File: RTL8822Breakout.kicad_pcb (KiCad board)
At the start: 2 copper layers, 35 x 35 mm, 11 parts, among them J1 U.FL, J2 U.FL, J3 Conn_02x09_Odd_Even, J4 Conn_02x09_Odd_Even, U1 RTL8822CS

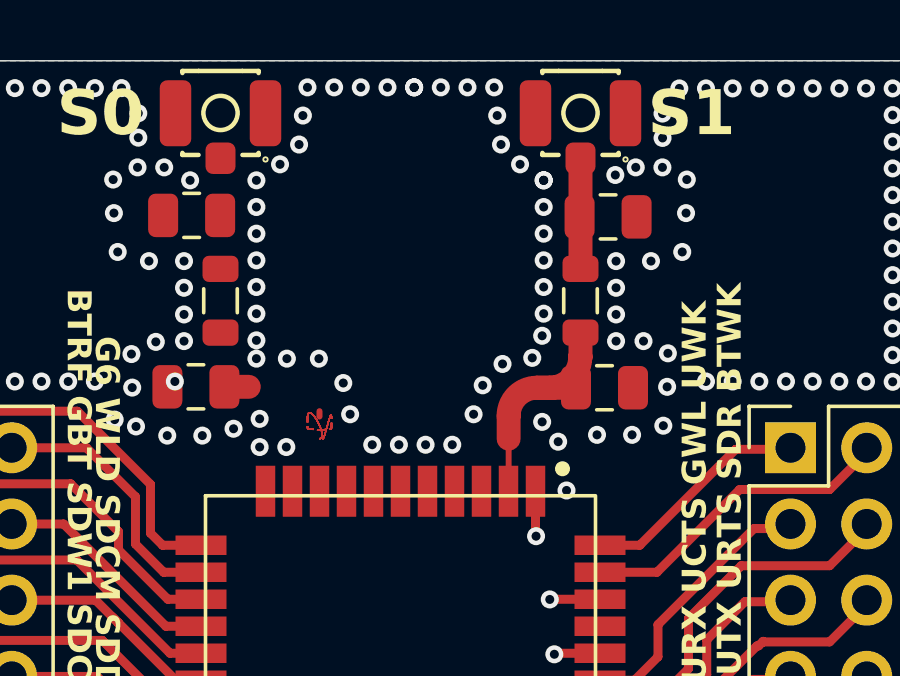
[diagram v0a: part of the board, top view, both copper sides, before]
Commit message: Added teardrops and removed the soldermask from RF tracks
Signed-off-by: Hotwater17 <michgor@o2.pl>
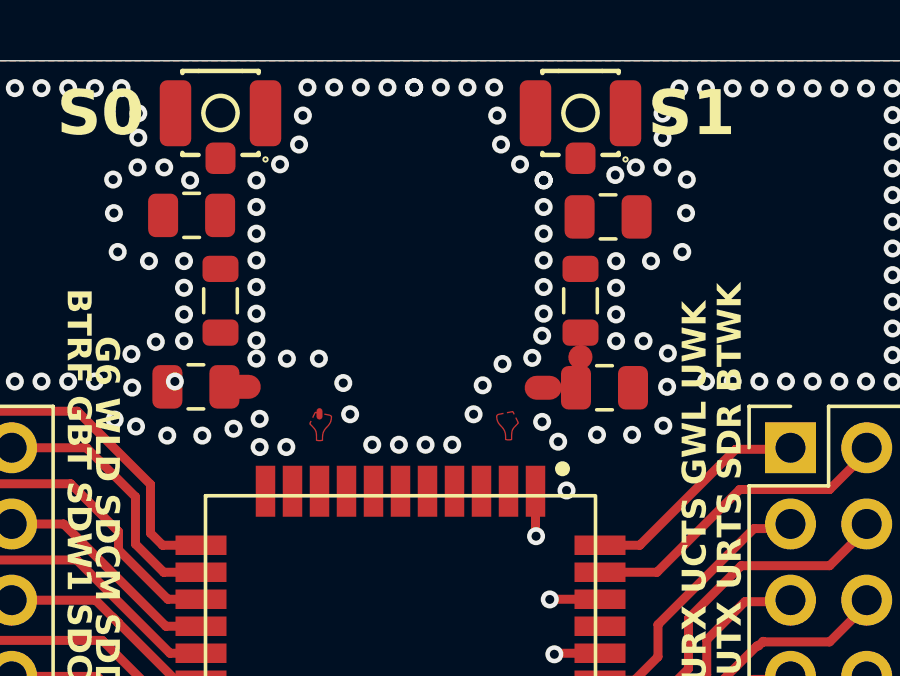
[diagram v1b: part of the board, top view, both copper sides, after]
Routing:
- net /S0: track 9.46 -> 8.67 mm
- net /S1: track 8.88 -> 8.12 mm
- added copper zone on F.Cu, net /S1
